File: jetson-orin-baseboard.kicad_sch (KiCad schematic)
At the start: 4 parts

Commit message: v2.0 Schematic updates
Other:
- company: Argus-1 Cubesat -> Carnegie Mellon University
- title: Jetson Carrier Board -> Argus Carrierboard
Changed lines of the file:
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@@
 	(paper "A4")
 	(title_block
-		(title "Jetson Carrier Board")
-		(date "2024-07-05")
-		(rev "v1")
-		(company "Argus-1 Cubesat")
+		(title "Argus Carrierboard")
+		(date "2025-03-10")
+		(rev "v2.0")
+		(company "Carnegie Mellon University")
 		(comment 1 "www.antmicro.com")
 		(comment 2 "N. Khera")

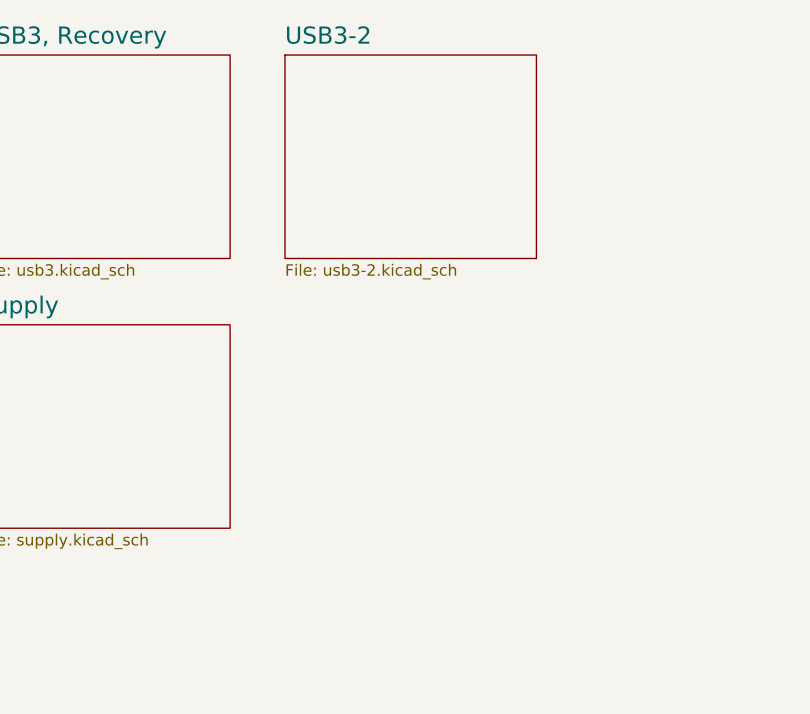
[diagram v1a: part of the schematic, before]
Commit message: v2.0 Layout completed. Exported BOM and STEP files
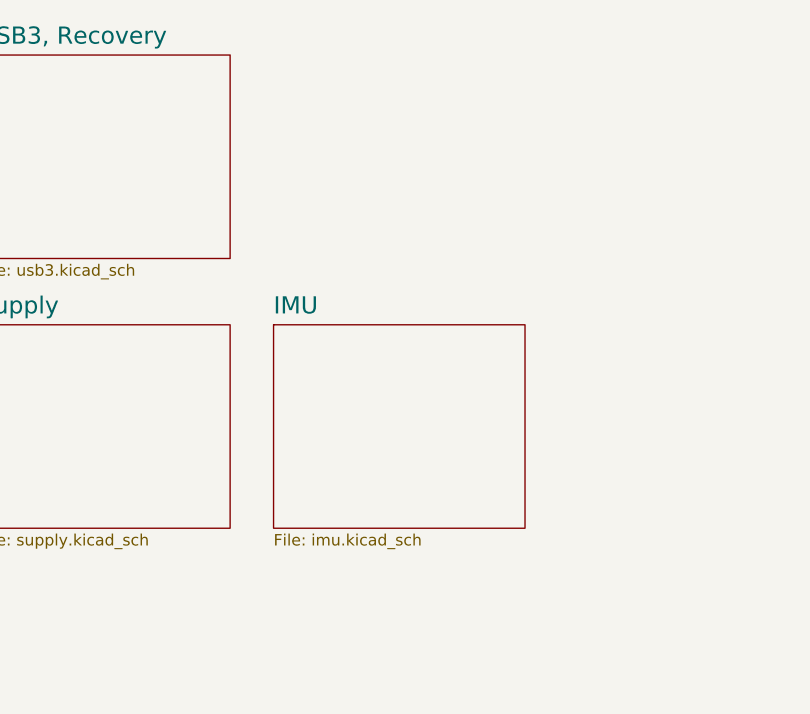
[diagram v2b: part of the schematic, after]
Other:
- removed sheet USB3-2
- added sheet IMU (imu.kicad_sch)
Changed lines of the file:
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@@
 (kicad_sch
-	(version 20231120)
+	(version 20250114)
 	(generator "eeschema")
-	(generator_version "8.0")
+	(generator_version "9.0")
 	(paper "A4")
 	(title_block
@@
 	)
 	(sheet
+		(at 199.39 103.632)
+		(size 27.94 22.606)
+		(exclude_from_sim no)
+		(in_bom yes)
+		(on_board yes)
+		(dnp no)
+		(fields_autoplaced yes)
+		(stroke
+			(width 0.1524)
+			(type solid)
+		)
+		(fill
+			(color 0 0 0 0.0000)
+		)
+		(property "Sheetname" "IMU"
+			(at 199.39 102.6029 0)
+			(effects
+				(font
+					(size 1.905 1.905)
+				)
+				(justify left bottom)
+			)
+		)
+		(property "Sheetfile" "imu.kicad_sch"
+			(at 199.39 126.8226 0)
+			(effects
+				(font
+					(size 1.27 1.27)
+				)
+				(justify left top)
+			)
+		)
+		(instances
+			(project "jetson-orin-baseboard"
+				(path "/4b393452-b11e-416e-bc83-918ae3cab2f1"
+					(page "10")
+				)
+			)
+		)
+	)
+	(sheet
 		(at 67.564 103.632)
 		(size 27.686 22.606)
+		(exclude_from_sim no)
+		(in_bom yes)
+		(on_board yes)
+		(dnp no)
 		(fields_autoplaced yes)
 		(stroke
@@
 		(at 166.624 73.66)
 		(size 27.94 22.606)
+		(exclude_from_sim no)
+		(in_bom yes)
+		(on_board yes)
+		(dnp no)
 		(fields_autoplaced yes)
 		(stroke
@@
 		(at 166.624 103.632)
 		(size 27.94 22.606)
+		(exclude_from_sim no)
+		(in_bom yes)
+		(on_board yes)
+		(dnp no)
 		(fields_autoplaced yes)
 		(stroke
@@
 		(at 67.564 73.66)
 		(size 27.94 22.606)
+		(exclude_from_sim no)
+		(in_bom yes)
+		(on_board yes)
+		(dnp no)
 		(fields_autoplaced yes)
 		(stroke
@@
 		(at 100.838 103.632)
 		(size 27.94 22.606)
+		(exclude_from_sim no)
+		(in_bom yes)
+		(on_board yes)
+		(dnp no)
 		(fields_autoplaced yes)
 		(stroke
@@
 				(path "/4b393452-b11e-416e-bc83-918ae3cab2f1"
 					(page "8")
-				)
-			)
-		)
-	)
-	(sheet
-		(at 200.66 73.66)
-		(size 27.94 22.606)
-		(fields_autoplaced yes)
-		(stroke
-			(width 0.1524)
-			(type solid)
-		)
-		(fill
-			(color 0 0 0 0.0000)
-		)
-		(property "Sheetname" "USB3-2"
-			(at 200.66 72.6309 0)
-			(effects
-				(font
-					(size 1.905 1.905)
-				)
-				(justify left bottom)
-			)
-		)
-		(property "Sheetfile" "usb3-2.kicad_sch"
-			(at 200.66 96.8506 0)
-			(effects
-				(font
-					(size 1.27 1.27)
-				)
-				(justify left top)
-			)
-		)
-		(instances
-			(project "jetson-orin-baseboard"
-				(path "/4b393452-b11e-416e-bc83-918ae3cab2f1"
-					(page "6")
 				)
 			)
@@
 		(at 100.838 73.66)
 		(size 27.94 22.606)
+		(exclude_from_sim no)
+		(in_bom yes)
+		(on_board yes)
+		(dnp no)
 		(fields_autoplaced yes)
 		(stroke
@@
 		(at 133.604 103.632)
 		(size 27.94 22.606)
+		(exclude_from_sim no)
+		(in_bom yes)
+		(on_board yes)
+		(dnp no)
 		(fields_autoplaced yes)
 		(stroke
@@
 		(at 133.604 73.66)
 		(size 27.94 22.606)
+		(exclude_from_sim no)
+		(in_bom yes)
+		(on_board yes)
+		(dnp no)
 		(fields_autoplaced yes)
 		(stroke
@@
 		)
 	)
+	(embedded_fonts no)
 )
